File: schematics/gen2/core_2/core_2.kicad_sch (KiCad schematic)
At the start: 13 parts, among them J1 Conn_02x25_Counter_Clockwise, U2 74LS574, U3 74LS02, U4 74LS04

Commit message: Add gen2/core_2
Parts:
- removed J1: Conn_02x25_Counter_Clockwise, Connector_PinSocket_2.54mm:PinSocket_2x25_P2.54mm_Horizontal, symbol Connector_Generic:Conn_02x25_Counter_Clockwise
- removed unit 5 of U4
- removed unit 1 of U4
- removed unit 4 of U4
- removed unit 6 of U4
- added BC1: BusConnector, Connector_PCBEdge:BUS_PCIexpress_x16, symbol cpu816symbols:BusConnector
- added C1, C17, C2, C3: C, symbol Device:C
- added R2, R3: R, symbol Device:R
- added STEP1: 74LS161, Package_DIP:DIP-16_W7.62mm_Socket_LongPads, symbol 74xx:74LS161
- added TABLE7, TABLE8: 28C256, Package_DIP:DIP-28_W15.24mm_Socket_LongPads, symbol Memory_EEPROM:28C256
- added unit 1 of U1
- added unit 5 of U1
- added unit 6 of U1
- added unit 4 of U1
- added unit 1 of U3
- added U5: 74LS00, Package_DIP:DIP-14_W7.62mm_Socket_LongPads, symbol 74xx:74LS00
- B_IN0, B_IN1, B_OUT0, U2: footprint (none) -> Package_DIP:DIP-20_W7.62mm_Socket_LongPads
- U1: renamed from U4; footprint (none) -> Package_DIP:DIP-14_W7.62mm_Socket_LongPads
- U3: footprint (none) -> Package_DIP:DIP-14_W7.62mm_Socket_LongPads
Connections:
- net D0: now also BC1.A51 (DATA0)
- net D1: now also BC1.A52 (DATA1)
- net D2: now also BC1.A53 (DATA2)
- net D3: now also BC1.A54 (DATA3)
- net D4: now also BC1.A55 (DATA4)
- net D5: now also BC1.A56 (DATA5)
- net D6: now also BC1.A57 (DATA6)
- net D7: now also BC1.A58 (DATA7)
- net GND: now also U3.12, BC1.A12 (GND), BC1.A13 (GND), BC1.A23 (GND), BC1.A32 (GND), BC1.A41 (GND), BC1.A50 (GND), BC1.A59 (GND), BC1.A63 (GND), BC1.A64 (GND), BC1.A65 (GND), BC1.A66 (GND), BC1.A70 (GND), BC1.A71 (GND), BC1.A72 (GND), BC1.A73 (GND), BC1.A74 (GND), BC1.A75 (GND), BC1.A76 (GND), BC1.B12 (GND), BC1.B13 (GND), BC1.B23 (GND), BC1.B32 (GND), BC1.B41 (GND), BC1.B50 (GND), BC1.B59 (GND), BC1.B62 (GND), BC1.B63 (GND), BC1.B64 (GND), BC1.B65 (GND), BC1.B66 (GND), BC1.B67 (GND), BC1.B68 (GND), BC1.B69 (GND), BC1.B70 (GND), BC1.B71 (GND), BC1.B72 (GND), BC1.B75 (GND), BC1.B76 (GND), C1.2, C17.2, C2.2, C3.2, STEP1.3 (D0), STEP1.4 (D1), STEP1.5 (D2), STEP1.6 (D3), STEP1.8 (GND), TABLE7.14 (GND), TABLE7.20 (~{CS}), TABLE7.27 (~{WE}), TABLE8.14 (GND), TABLE8.20 (~{CS}), TABLE8.27 (~{WE}), U3.3, U5.7 (GND)
- net SignIn: now also BC1.A62 (ALUSO)
- net VCC: now also BC1.A1 (VCC), BC1.A2 (VCC), BC1.A3 (VCC), BC1.A4 (VCC), BC1.A5 (VCC), BC1.B1 (VCC), BC1.B2 (VCC), BC1.B3 (VCC), BC1.B4 (VCC), BC1.B5 (VCC), C1.1, C17.1, C2.1, C3.1, R2.1, R3.1, STEP1.16 (VCC), TABLE7.28 (VCC), TABLE8.28 (VCC), U5.14 (VCC)
- net ZeroIn: now also BC1.A60 (ALUZO)
- net ~CLK: now also BC1.B73 (~{CLK}), U1.11, U5.13
- net ~{CarryIn}: now also BC1.A61 (~{ALUCO})
- net ~{LOAD_FR}: now also B_IN1.19 (CE), BC1.A28 (~{LFR})
- net ~{OUT_FR}: now also BC1.B28 (~{RFR})
- net ~{UPDATE_FR}: now also BC1.B39 (FRUpd); no longer B_IN1.19 (CE)
- net at U3.11: now also R3.2
- net SignOut renamed STATE8
- net STATE8: now also BC1.A42 (STATE8), TABLE7.25 (A8), TABLE8.25 (A8)
- net ZeroOut renamed STATE10
- net STATE10: now also BC1.A44 (STATE10), TABLE7.21 (A10), TABLE8.21 (A10)
- net ~{CarryOut} renamed STATE9
- net STATE9: now also BC1.A43 (STATE9), TABLE7.24 (A9), TABLE8.24 (A9)
- new net: STEP1.1 (~{MR}), U5.6
- new net: STEP1.10 (CET), STEP1.7 (CEP), U5.3
- new net: TABLE8.22 (~{OE}), U1.2
- new net: R2.2, U3.2
- new net: BC1.B74 (PULSE), U5.11
- new net: U1.8, U5.12
- new net: U5.1, U5.2, U5.8
- new net: U1.12, U1.9
- new net AddrDecrement: BC1.B60 (ADRDEC), TABLE7.13 (D2), TABLE8.13 (D2)
- new net AddrIncrement: BC1.B61 (ADDRINC), TABLE7.15 (D3), TABLE8.15 (D3)
- new net Clk: STEP1.2 (CP), U1.10, U1.13
- new net IntEnable: BC1.B57 (INTE), TABLE7.11 (D0), TABLE8.11 (D0)
- new net Reset: BC1.A69 (RESET), U5.4, U5.5
- new net STATE0: BC1.A33 (STATE0), TABLE7.10 (A0), TABLE8.10 (A0)
- new net STATE1: BC1.A34 (STATE1), TABLE7.9 (A1), TABLE8.9 (A1)
- new net STATE11: BC1.A45 (STATE11), STEP1.14 (Q0), TABLE7.23 (A11), TABLE8.23 (A11)
- new net STATE12: BC1.A46 (STATE12), STEP1.13 (Q1), TABLE7.2 (A12), TABLE8.2 (A12)
- new net STATE13: BC1.A47 (STATE13), STEP1.12 (Q2), TABLE7.26 (A13), TABLE8.26 (A13)
- new net STATE14: BC1.A48 (STATE14), STEP1.11 (Q3), TABLE7.1 (A14), TABLE8.1 (A14)
- new net STATE15: BC1.A49 (STATE15), TABLE7.22 (~{OE}), U1.1
- new net STATE2: BC1.A35 (STATE2), TABLE7.8 (A2), TABLE8.8 (A2)
- new net STATE3: BC1.A36 (STATE3), TABLE7.7 (A3), TABLE8.7 (A3)
- new net STATE4: BC1.A37 (STATE4), TABLE7.6 (A4), TABLE8.6 (A4)
- new net STATE5: BC1.A38 (STATE5), TABLE7.5 (A5), TABLE8.5 (A5)
- new net STATE6: BC1.A39 (STATE6), TABLE7.4 (A6), TABLE8.4 (A6)
- new net STATE7: BC1.A40 (STATE7), TABLE7.3 (A7), TABLE8.3 (A7)
- new net ~{Halt}: BC1.B46 (~{HALT}), U5.9
- new net ~{IntDisable}: BC1.B58 (~{INTD}), TABLE7.12 (D1), TABLE8.12 (D1)
- new net ~{SCClear}: BC1.B45 (~{SCCLR}), STEP1.9 (~{PE})
- new net ~{Wait}: BC1.A68 (~{WAIT}), U5.10
- no-connect marks 34 -> 63
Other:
- moved on the sheet: U3D

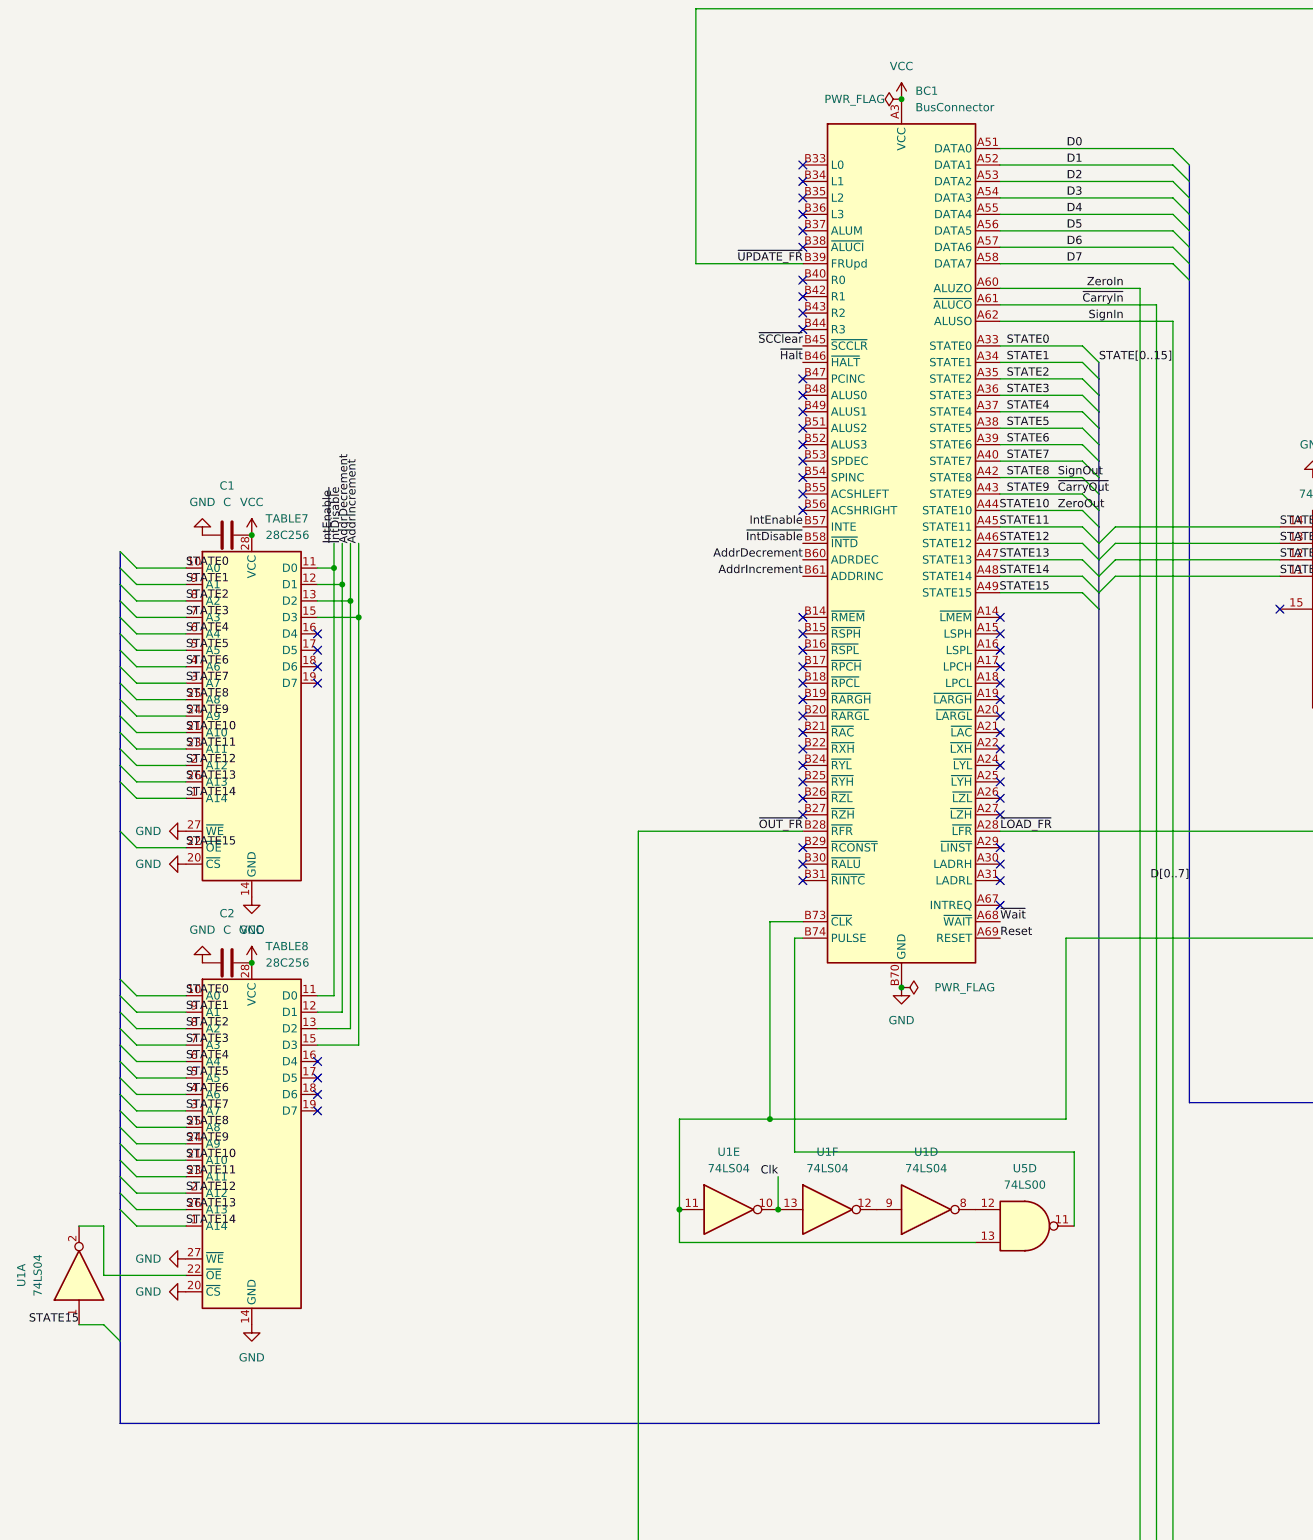
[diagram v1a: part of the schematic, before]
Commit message: Add core3, fix core2
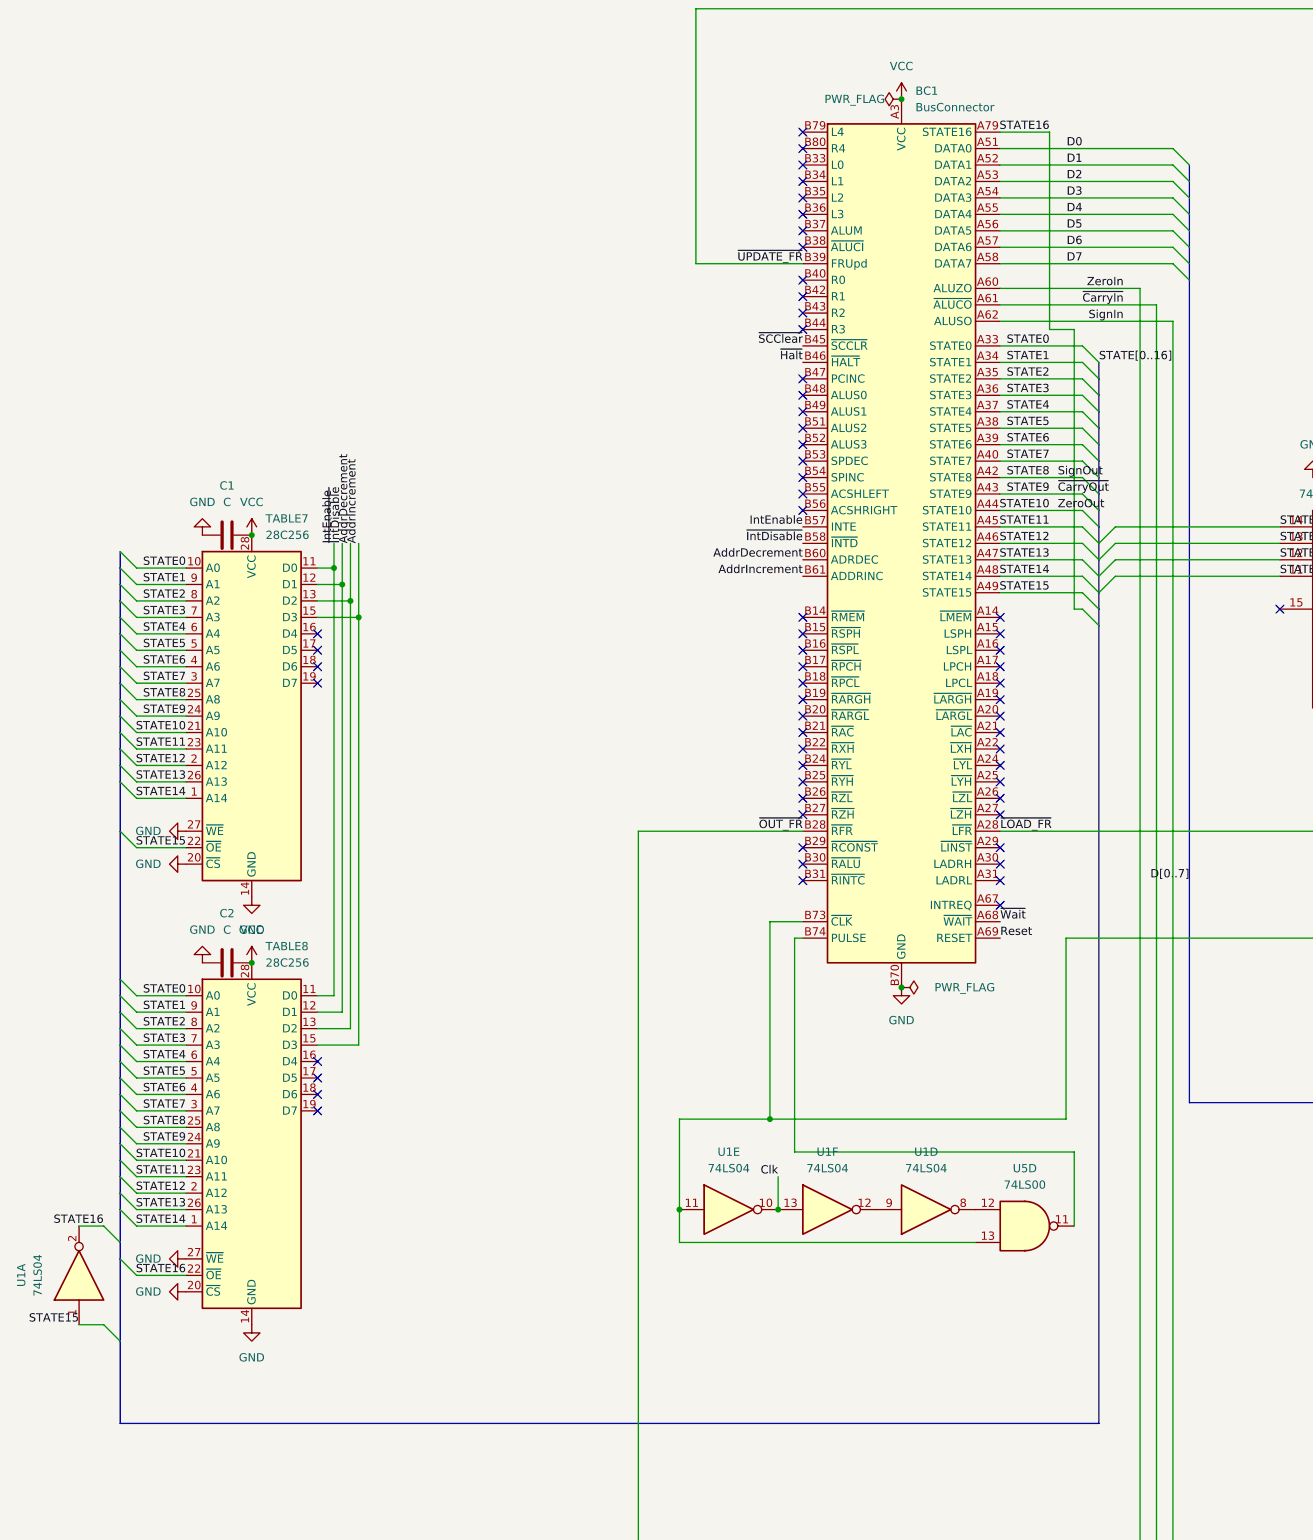
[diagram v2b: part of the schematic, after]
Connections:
- net STATE16: now reaches TABLE8.22 (~{OE}), U1.2
- net STATE16: now also BC1.A79 (STATE16)
- no-connect marks 63 -> 65

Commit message: almost ready core 2
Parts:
- removed R3: R, symbol Device:R
- C1, C11, C12, C17, C2, C3, C6, C7, C8, C9: footprint (none) -> Capacitor_THT:C_Disc_D5.0mm_W2.5mm_P5.00mm
- R2: footprint (none) -> Resistor_THT:R_Axial_DIN0207_L6.3mm_D2.5mm_P7.62mm_Horizontal
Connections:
- net GND: no longer U3.12, U3.3
- net at R2.2, U3.2: now also U3.11, U3.12, U3.3
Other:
- moved on the sheet: BC1, B_IN0, B_IN1, B_OUT0, C1, C11, C12, C17, C2, C3, C6, C8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

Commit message: doine(core_ 2): almost ready to print
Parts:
- added C4: C, Capacitor_THT:C_Radial_D6.3mm_H5.0mm_P2.50mm, symbol Device:C
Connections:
- net GND: now also C4.2
- net VCC: now also C4.1
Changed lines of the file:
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@@
 	)
 	(junction
+		(at 215.9 55.88)
+		(diameter 0)
+		(color 0 0 0 0)
+	)
+	(junction
 		(at 309.88 262.89)
 		(diameter 0)
@@
 	(wire
 		(pts
+			(xy 215.9 53.34) (xy 215.9 55.88)
+		)
+		(stroke
+			(width 0)
+			(type default)
+		)
+	)
+	(wire
+		(pts
 			(xy 300.99 125.73) (xy 303.53 125.73)
 		)
@@
 	(wire
 		(pts
+			(xy 215.9 55.88) (xy 215.9 59.69)
+		)
+		(stroke
+			(width 0)
+			(type default)
+		)
+	)
+	(wire
+		(pts
 			(xy 231.14 93.98) (xy 257.81 93.98)
 		)
@@
 	)
 	(symbol
+		(lib_id "power:GND")
+		(at 223.52 55.88 0)
+		(unit 1)
+		(exclude_from_sim no)
+		(in_bom yes)
+		(on_board yes)
+		(dnp no)
+		(property "Reference" "#PWR021"
+			(at 223.52 62.23 0)
+			(effects
+				(font
+					(size 1.27 1.27)
+				)
+				(hide yes)
+			)
+		)
+		(property "Value" "GND"
+			(at 227.076 56.134 0)
+			(effects
+				(font
+					(size 1.27 1.27)
+				)
+			)
+		)
+		(property "Footprint" ""
+			(at 223.52 55.88 0)
+			(effects
+				(font
+					(size 1.27 1.27)
+				)
+				(hide yes)
+			)
+		)
+		(property "Datasheet" ""
+			(at 223.52 55.88 0)
+			(effects
+				(font
+					(size 1.27 1.27)
+				)
+				(hide yes)
+			)
+		)
+		(property "Description" "Power symbol creates a global label with name \"GND\" , ground"
+			(at 223.52 55.88 0)
+			(effects
+				(font
+					(size 1.27 1.27)
+				)
+				(hide yes)
+			)
+		)
+		(pin "1"
+		)
+		(instances
+			(project ""
+				(path "/59b2db81-41fa-4862-96ef-fb4ce3ab7be6"
+					(reference "#PWR021")
+					(unit 1)
+				)
+			)
+		)
+	)
+	(symbol
 		(lib_id "74xx:74LS574")
 		(at 414.02 284.48 0)
@@
 	)
 	(symbol
+		(lib_id "Device:C")
+		(at 219.71 55.88 90)
+		(unit 1)
+		(exclude_from_sim no)
+		(in_bom yes)
+		(on_board yes)
+		(dnp no)
+		(fields_autoplaced yes)
+		(property "Reference" "C4"
+			(at 219.71 48.26 90)
+			(effects
+				(font
+					(size 1.27 1.27)
+				)
+			)
+		)
+		(property "Value" "C"
+			(at 219.71 50.8 90)
+			(effects
+				(font
+					(size 1.27 1.27)
+				)
+			)
+		)
+		(property "Footprint" "Capacitor_THT:C_Radial_D6.3mm_H5.0mm_P2.50mm"
+			(at 223.52 54.9148 0)
+			(effects
+				(font
+					(size 1.27 1.27)
+				)
+				(hide yes)
+			)
+		)
+		(property "Datasheet" "~"
+			(at 219.71 55.88 0)
+			(effects
+				(font
+					(size 1.27 1.27)
+				)
+				(hide yes)
+			)
+		)
+		(property "Description" "Unpolarized capacitor"
+			(at 219.71 55.88 0)
+			(effects
+				(font
+					(size 1.27 1.27)
+				)
+				(hide yes)
+			)
+		)
+		(pin "2"
+		)
+		(pin "1"
+		)
+		(instances
+			(project ""
+				(path "/59b2db81-41fa-4862-96ef-fb4ce3ab7be6"
+					(reference "C4")
+					(unit 1)
+				)
+			)
+		)
+	)
+	(symbol
 		(lib_id "74xx:74LS245")
 		(at 309.88 284.48 0)
@@
 	(symbol
 		(lib_id "power:VCC")
-		(at 215.9 59.69 0)
+		(at 215.9 53.34 0)
 		(unit 1)
 		(exclude_from_sim no)
@@
 		(fields_autoplaced yes)
 		(property "Reference" "#PWR07"
-			(at 215.9 63.5 0)
+			(at 215.9 57.15 0)
 			(effects
 				(font
@@
 		)
 		(property "Value" "VCC"
-			(at 215.9 54.61 0)
+			(at 215.9 48.26 0)
 			(effects
 				(font
@@
 		)
 		(property "Footprint" ""
-			(at 215.9 59.69 0)
+			(at 215.9 53.34 0)
 			(effects
 				(font
@@
 		)
 		(property "Datasheet" ""
-			(at 215.9 59.69 0)
+			(at 215.9 53.34 0)
 			(effects
 				(font
@@
 		)
 		(property "Description" "Power symbol creates a global label with name \"VCC\""
-			(at 215.9 59.69 0)
+			(at 215.9 53.34 0)
 			(effects
 				(font
